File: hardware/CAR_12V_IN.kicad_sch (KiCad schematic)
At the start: 15 parts, among them J9 684M7W2103L461, Q26 NTA7002NT1G, Q27 AON7421

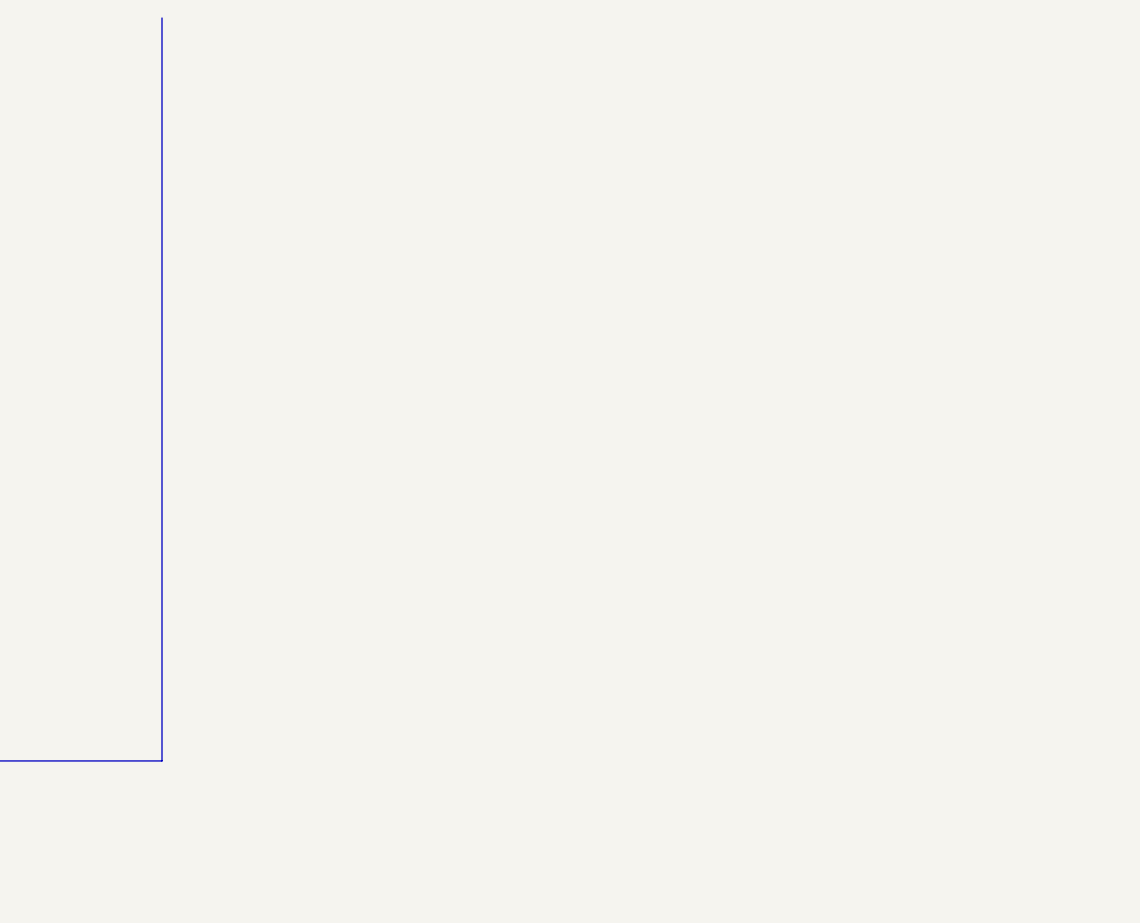
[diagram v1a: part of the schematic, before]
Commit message: switched can tranceiver to combo controler and tranceiver
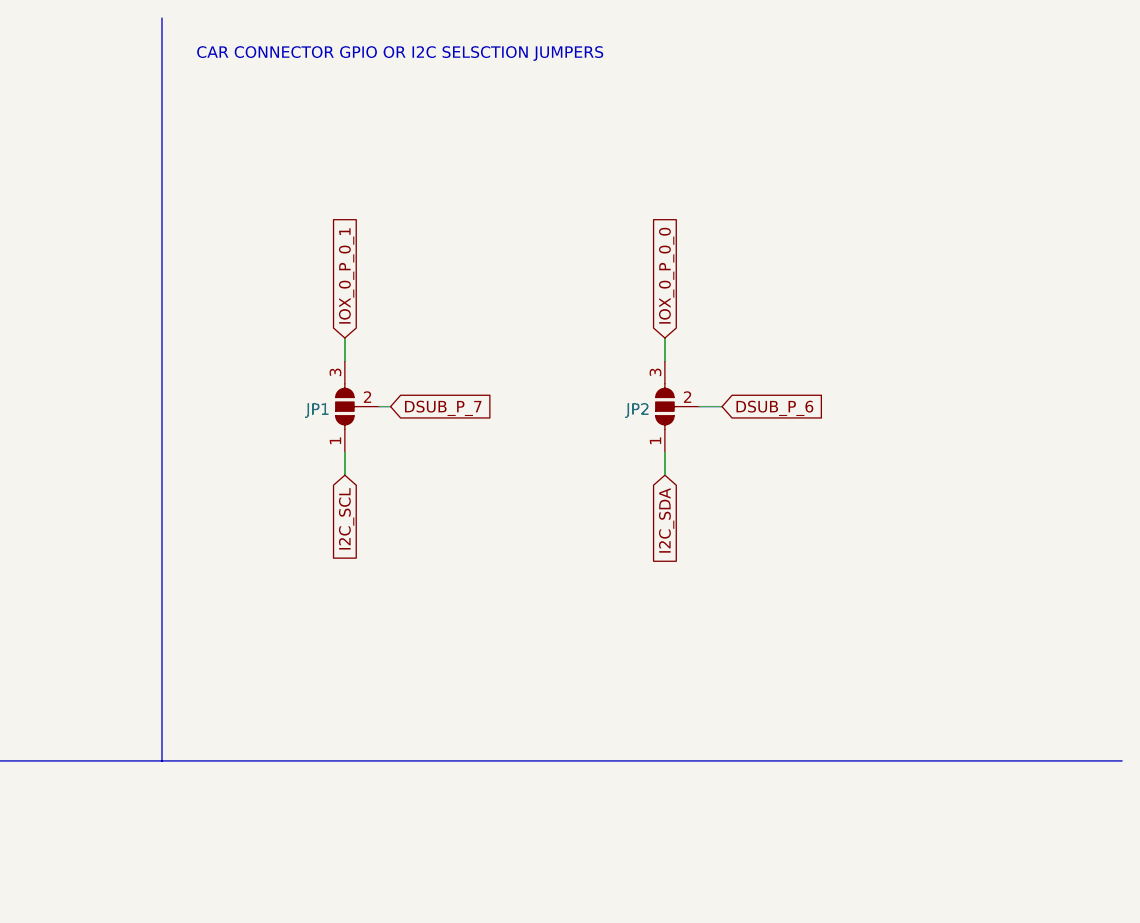
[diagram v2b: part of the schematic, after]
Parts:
- added JP1, JP2: ~, Jumper:SolderJumper-3_P1.3mm_Open_RoundedPad1.0x1.5mm_NumberLabels, symbol Jumper:SolderJumper_3_Open
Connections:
- net DSUB_P_6: now also JP2.2 (C)
- net DSUB_P_7: now also JP1.2 (C)
- new net I2C_SCL: JP1.1 (A)
- new net I2C_SDA: JP2.1 (A)
- new net IOX_0_P_0_0: JP2.3 (B)
- new net IOX_0_P_0_1: JP1.3 (B)
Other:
- note added: "CAR CONNECTOR GPIO OR I2C SELSCTION JUMPERS"

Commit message: migrated to the esp32-s2 and starting new board revison
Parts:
- renumbered C112 to C131, H1 to H2, H1 to H3, H1 to H4, H1 to H5, H1 to H6, H1 to H7, H1 to H8, JP1 to JP12, JP2 to JP13, Q27 to Q29, Q26 to Q30, R105 to R108, R107 to R109, R104 to R110
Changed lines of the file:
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@@
 (kicad_sch
-	(version 20231120)
+	(version 20250114)
 	(generator "eeschema")
-	(generator_version "8.0")
+	(generator_version "9.0")
 	(paper "A4")
 	(title_block
@@
 		(comment 3 "TOTAL SYSTEM POWER IS ~275w")
 	)
+	(text "CAR CONNECTOR GPIO OR I2C SELSCTION JUMPERS"
+		(exclude_from_sim no)
+		(at 181.61 16.256 0)
+		(effects
+			(font
+				(size 1.27 1.27)
+			)
+			(justify left bottom)
+		)
+	)
+	(text "SHELD LINK"
+		(exclude_from_sim no)
+		(at 15.24 100.33 0)
+		(effects
+			(font
+				(size 1.27 1.27)
+			)
+			(justify left bottom)
+		)
+	)
+	(text "CAR CONNECTOR"
+		(exclude_from_sim no)
+		(at 13.97 17.78 0)
+		(effects
+			(font
+				(size 1.27 1.27)
+			)
+			(justify left bottom)
+		)
+	)
+	(text "MOUNTING HOLES"
+		(exclude_from_sim no)
+		(at 128.27 17.78 0)
+		(effects
+			(font
+				(size 1.27 1.27)
+			)
+			(justify left bottom)
+		)
+	)
 	(junction
 		(at 62.23 115.57)
@@
 		)
 	)
-	(text "CAR CONNECTOR GPIO OR I2C SELSCTION JUMPERS"
-		(exclude_from_sim no)
-		(at 181.61 16.256 0)
-		(effects
-			(font
-				(size 1.27 1.27)
-			)
-			(justify left bottom)
-		)
-	)
-	(text "SHELD LINK"
-		(exclude_from_sim no)
-		(at 15.24 100.33 0)
-		(effects
-			(font
-				(size 1.27 1.27)
-			)
-			(justify left bottom)
-		)
-	)
-	(text "CAR CONNECTOR"
-		(exclude_from_sim no)
-		(at 13.97 17.78 0)
-		(effects
-			(font
-				(size 1.27 1.27)
-			)
-			(justify left bottom)
-		)
-	)
-	(text "MOUNTING HOLES"
-		(exclude_from_sim no)
-		(at 128.27 17.78 0)
-		(effects
-			(font
-				(size 1.27 1.27)
-			)
-			(justify left bottom)
-		)
-	)
 	(global_label "DSUB_P_6"
 		(shape input)
@@
 		(dnp no)
 		(fields_autoplaced yes)
-		(property "Reference" "R104"
+		(property "Reference" "R110"
 			(at 53.34 111.5441 90)
 			(effects
@@
 			(project "usbc-car-module"
 				(path "/fae025e9-99c5-40c1-af6f-99dc1edbfa43/67a132ab-d248-4cef-8ed8-9da8a5ccfd64"
-					(reference "R104")
+					(reference "R110")
 					(unit 1)
 				)
@@
 		(dnp no)
 		(fields_autoplaced yes)
-		(property "Reference" "#PWR0142"
+		(property "Reference" "#PWR0152"
 			(at 44.45 86.36 0)
 			(effects
@@
 			(project "usbc-car-module"
 				(path "/fae025e9-99c5-40c1-af6f-99dc1edbfa43/67a132ab-d248-4cef-8ed8-9da8a5ccfd64"
-					(reference "#PWR0142")
+					(reference "#PWR0152")
 					(unit 1)
 				)
@@
 		(dnp no)
 		(fields_autoplaced yes)
-		(property "Reference" "H1"
+		(property "Reference" "H6"
 			(at 142.24 49.9653 0)
 			(effects
@@
 			(project "usbc-car-module"
 				(path "/fae025e9-99c5-40c1-af6f-99dc1edbfa43/67a132ab-d248-4cef-8ed8-9da8a5ccfd64"
-					(reference "H1")
+					(reference "H6")
 					(unit 1)
 				)
@@
 		(dnp no)
 		(fields_autoplaced yes)
-		(property "Reference" "H1"
+		(property "Reference" "H7"
 			(at 142.24 55.0453 0)
 			(effects
@@
 			(project "usbc-car-module"
 				(path "/fae025e9-99c5-40c1-af6f-99dc1edbfa43/67a132ab-d248-4cef-8ed8-9da8a5ccfd64"
-					(reference "H8")
+					(reference "H7")
 					(unit 1)
 				)
@@
 		(dnp no)
 		(fields_autoplaced yes)
-		(property "Reference" "C112"
+		(property "Reference" "C131"
 			(at 53.34 102.7811 90)
 			(effects
@@
 			(project "usbc-car-module"
 				(path "/fae025e9-99c5-40c1-af6f-99dc1edbfa43/67a132ab-d248-4cef-8ed8-9da8a5ccfd64"
-					(reference "C112")
+					(reference "C131")
 					(unit 1)
 				)
@@
 			(project "usbc-car-module"
 				(path "/fae025e9-99c5-40c1-af6f-99dc1edbfa43/67a132ab-d248-4cef-8ed8-9da8a5ccfd64"
-					(reference "H7")
+					(reference "H1")
 					(unit 1)
 				)
@@
 		(dnp no)
 		(fields_autoplaced yes)
-		(property "Reference" "R107"
+		(property "Reference" "R109"
 			(at 74.168 60.3163 0)
 			(effects
@@
 			(project "usbc-car-module"
 				(path "/fae025e9-99c5-40c1-af6f-99dc1edbfa43/67a132ab-d248-4cef-8ed8-9da8a5ccfd64"
-					(reference "R107")
+					(reference "R109")
 					(unit 1)
 				)
@@
 		(dnp no)
 		(fields_autoplaced yes)
-		(property "Reference" "H1"
+		(property "Reference" "H5"
 			(at 142.24 44.8853 0)
 			(effects
@@
 			(project "usbc-car-module"
 				(path "/fae025e9-99c5-40c1-af6f-99dc1edbfa43/67a132ab-d248-4cef-8ed8-9da8a5ccfd64"
-					(reference "H3")
+					(reference "H5")
 					(unit 1)
 				)
@@
 		(dnp no)
 		(fields_autoplaced yes)
-		(property "Reference" "Q27"
+		(property "Reference" "Q29"
 			(at 87.63 35.7251 90)
 			(effects
@@
 			(project "usbc-car-module"
 				(path "/fae025e9-99c5-40c1-af6f-99dc1edbfa43/67a132ab-d248-4cef-8ed8-9da8a5ccfd64"
-					(reference "Q27")
+					(reference "Q29")
 					(unit 1)
 				)
@@
 		(dnp no)
 		(fields_autoplaced yes)
-		(property "Reference" "#PWR0143"
+		(property "Reference" "#PWR0153"
 			(at 45.72 125.73 0)
 			(effects
@@
 			(project "usbc-car-module"
 				(path "/fae025e9-99c5-40c1-af6f-99dc1edbfa43/67a132ab-d248-4cef-8ed8-9da8a5ccfd64"
-					(reference "#PWR0143")
+					(reference "#PWR0153")
 					(unit 1)
 				)
@@
 		(dnp no)
 		(fields_autoplaced yes)
-		(property "Reference" "JP2"
+		(property "Reference" "JP13"
 			(at 232.029 54.9268 90)
 			(effects
@@
 			(project "usbc-car-module"
 				(path "/fae025e9-99c5-40c1-af6f-99dc1edbfa43/67a132ab-d248-4cef-8ed8-9da8a5ccfd64"
-					(reference "JP2")
+					(reference "JP13")
 					(unit 1)
 				)
@@
 		(dnp no)
 		(fields_autoplaced yes)
-		(property "Reference" "R105"
+		(property "Reference" "R108"
 			(at 76.708 45.0763 0)
 			(effects
@@
 			(project "usbc-car-module"
 				(path "/fae025e9-99c5-40c1-af6f-99dc1edbfa43/67a132ab-d248-4cef-8ed8-9da8a5ccfd64"
-					(reference "R105")
+					(reference "R108")
 					(unit 1)
 				)
@@
 		(dnp no)
 		(fields_autoplaced yes)
-		(property "Reference" "H1"
+		(property "Reference" "H2"
 			(at 142.24 29.6453 0)
 			(effects
@@
 			(project "usbc-car-module"
 				(path "/fae025e9-99c5-40c1-af6f-99dc1edbfa43/67a132ab-d248-4cef-8ed8-9da8a5ccfd64"
-					(reference "H9")
+					(reference "H2")
 					(unit 1)
 				)
@@
 		(dnp no)
 		(fields_autoplaced yes)
-		(property "Reference" "#PWR0144"
+		(property "Reference" "#PWR0154"
 			(at 62.23 125.73 0)
 			(effects
@@
 			(project "usbc-car-module"
 				(path "/fae025e9-99c5-40c1-af6f-99dc1edbfa43/67a132ab-d248-4cef-8ed8-9da8a5ccfd64"
-					(reference "#PWR0144")
+					(reference "#PWR0154")
 					(unit 1)
 				)
@@
 		(dnp no)
 		(fields_autoplaced yes)
-		(property "Reference" "H1"
+		(property "Reference" "H3"
 			(at 142.24 34.7253 0)
 			(effects
@@
 			(project "usbc-car-module"
 				(path "/fae025e9-99c5-40c1-af6f-99dc1edbfa43/67a132ab-d248-4cef-8ed8-9da8a5ccfd64"
-					(reference "H4")
+					(reference "H3")
 					(unit 1)
 				)
@@
 		(dnp no)
 		(fields_autoplaced yes)
-		(property "Reference" "H1"
+		(property "Reference" "H4"
 			(at 142.24 39.8053 0)
 			(effects
@@
 			(project "usbc-car-module"
 				(path "/fae025e9-99c5-40c1-af6f-99dc1edbfa43/67a132ab-d248-4cef-8ed8-9da8a5ccfd64"
-					(reference "H2")
+					(reference "H4")
 					(unit 1)
 				)
@@
 		(dnp no)
 		(fields_autoplaced yes)
-		(property "Reference" "H1"
+		(property "Reference" "H8"
 			(at 142.24 60.1253 0)
 			(effects
@@
 			(project "usbc-car-module"
 				(path "/fae025e9-99c5-40c1-af6f-99dc1edbfa43/67a132ab-d248-4cef-8ed8-9da8a5ccfd64"
-					(reference "H5")
+					(reference "H8")
 					(unit 1)
 				)
@@
 		(dnp no)
 		(fields_autoplaced yes)
-		(property "Reference" "JP1"
+		(property "Reference" "JP12"
 			(at 196.469 54.9268 90)
 			(effects
@@
 			(project "usbc-car-module"
 				(path "/fae025e9-99c5-40c1-af6f-99dc1edbfa43/67a132ab-d248-4cef-8ed8-9da8a5ccfd64"
-					(reference "JP1")
+					(reference "JP12")
 					(unit 1)
 				)
@@
 		(dnp no)
 		(fields_autoplaced yes)
-		(property "Reference" "#PWR0145"
+		(property "Reference" "#PWR0151"
 			(at 73.66 71.12 0)
 			(effects
@@
 			(project "usbc-car-module"
 				(path "/fae025e9-99c5-40c1-af6f-99dc1edbfa43/67a132ab-d248-4cef-8ed8-9da8a5ccfd64"
-					(reference "#PWR0145")
+					(reference "#PWR0151")
 					(unit 1)
 				)
@@
 		(dnp no)
 		(fields_autoplaced yes)
-		(property "Reference" "Q26"
+		(property "Reference" "Q30"
 			(at 90.297 57.7763 0)
 			(effects
@@
 			(project "usbc-car-module"
 				(path "/fae025e9-99c5-40c1-af6f-99dc1edbfa43/67a132ab-d248-4cef-8ed8-9da8a5ccfd64"
-					(reference "Q26")
-					(unit 1)
-				)
+					(reference "Q30")
+					(unit 1)
+				)
